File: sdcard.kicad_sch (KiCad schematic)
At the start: 20 parts, among them J9 microSD push-pull, Q2 -20V 2.3A P-ch, Q3 60V 300mA N-ch

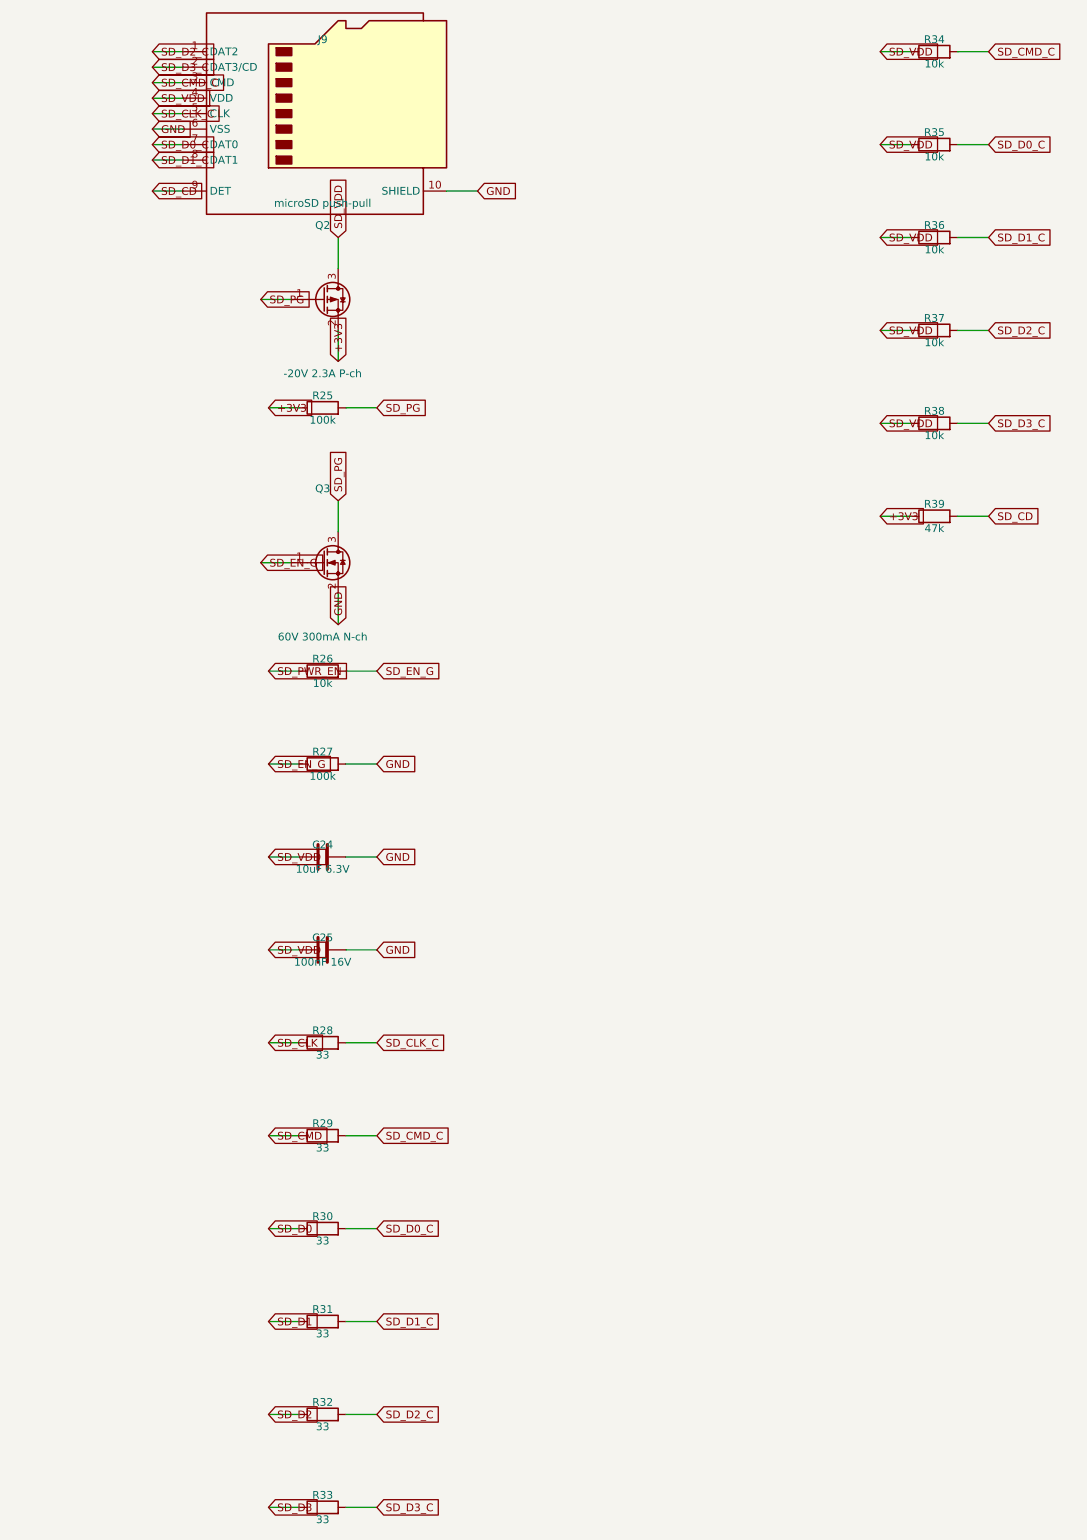
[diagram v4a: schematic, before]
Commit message: Schematic: power symbols and readable text placement (items 1-2 of 5)
The schematic was a netlist drawn as a picture: 486 global labels for 108
nets, roughly four per net, every part an island with a name flag on each
pin and no wires between anything. You could not trace a circuit by eye.
That is a fair description of a document that fails at the one thing a
schematic is for, and it is on me -- the generator was built to produce a
correct netlist and the drawing was an afterthought.

Two of the five agreed fixes are in:

Rails are power symbols. GND, +3V3, +5V, +5VS, +VBAT, VBUS and SD_VDD now
carry a proper power symbol instead of a net-name label -- 190 of them,
taking the label count from 486 to 296. Where KiCad has no stock symbol
for a rail a generic one is instantiated with its Value overridden, which
is how KiCad names a power net; validate.py re-extracts through KiCad and
compares node-for-node, so a wrong guess there would fail the build rather
than quietly merge two rails. PWR_FLAG keeps a label: pairing it with a
power symbol makes an island of two symbols that declares a rail and
connects to nothing visible.

Text no longer collides. Labels were all justified left, so any label
pointing back at its own component ran its text over the body -- RON_5V
across R4, SW_5V across L1; they now justify away from the part.
Reference and value sat hard against the symbol, so a pin leaving the top
or bottom put its stub and power symbol straight through them: "LM5164
(5V)" printed through the GND symbol under U2. Both now clear the stub,
and the row height accounts for it so the clearance does not just push
the collision into the next row. Power symbol references are hidden, as
they are in every schematic.

Also fixed: the packer wrapped on height but never on width, so the power
sheet silently ran off the 420 mm page -- two symbols landed at x = 422.9
where ERC reported them unconnected and nothing else complained. It now
fails loudly.

Items 3-5 (real hierarchy, w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
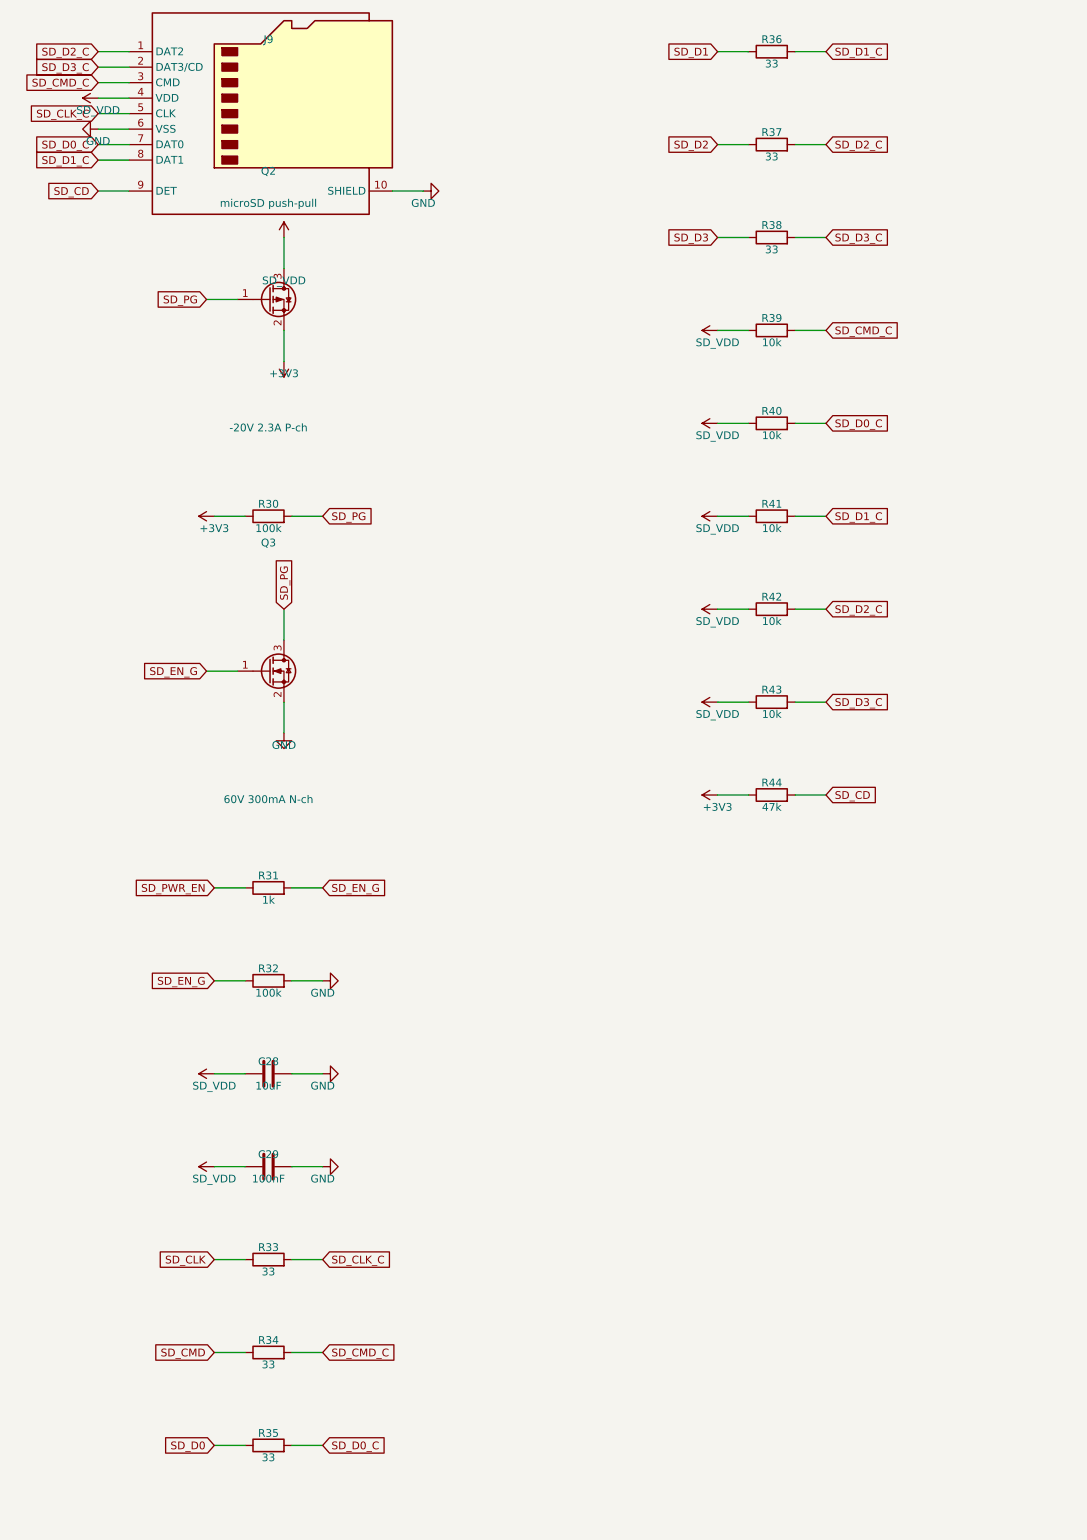
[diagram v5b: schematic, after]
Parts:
- removed C24: 10uF 6.3V, Capacitor_SMD:C_1206_3216Metric, symbol Device:C
- removed C25: 100nF 16V, Capacitor_SMD:C_0805_2012Metric, symbol Device:C
- removed R25, R27: 100k, Resistor_SMD:R_0805_2012Metric, symbol Device:R
- removed R26: 10k, Resistor_SMD:R_0805_2012Metric, symbol Device:R
- removed R28, R29: 33, Resistor_SMD:R_0805_2012Metric, symbol Device:R
- added C28: 10uF, Capacitor_SMD:C_1206_3216Metric, symbol Device:C
- added C29: 100nF, Capacitor_SMD:C_0805_2012Metric, symbol Device:C
- added R40, R41, R42, R43: 10k, Resistor_SMD:R_0805_2012Metric, symbol Device:R
- added R44: 47k, Resistor_SMD:R_0805_2012Metric, symbol Device:R
- Q3: Note Level shift for the P-ch gate -> Level shift for the P-ch gate. Prefer an AEC-Q101 equivalen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
- R30: value 33 -> 100k; Note Series damping -> Default off
- R31: value 33 -> 1k; Note Series damping -> Series gate resistor. 10k here divided against R27 100k and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
- R32: value 33 -> 100k; Note Series damping -> (none)
- R34, R35, R36, R37, R38: value 10k -> 33; Note Espressif's recommended value; pulled to the switched rail 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 -> Series damping
- R39: value 47k -> 10k; Note Card-detect pull-up -> Espressif's recommended value; pulled to the switched rail 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
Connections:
- net +3V3: now also R30.1, R44.1; no longer R39.1
- net GND: now also R32.2, C28.2, C29.2
- net SD_CD: now also R44.2; no longer R39.2
- net SD_CLK: now also R33.1
- net SD_CLK_C: now also R33.2
- net SD_CMD: now also R34.1
- net SD_CMD_C: now also R39.2
- net SD_D0: now also R35.1; no longer R30.1
- net SD_D0_C: now also R40.2; no longer R30.2
- net SD_D1: now also R36.1; no longer R31.1
- net SD_D1_C: now also R41.2; no longer R31.2
- net SD_D2: now also R37.1; no longer R32.1
- net SD_D2_C: now also R42.2; no longer R32.2
- net SD_D3: now also R38.1; no longer R33.1
- net SD_D3_C: now also R43.2; no longer R33.2
- net SD_EN_G: now also R31.2, R32.1
- net SD_PG: now also R30.2
- net SD_PWR_EN: now also R31.1
- net SD_VDD: now also R39.1, C28.1, C29.1, R40.1, R41.1, R42.1, R43.1; no longer R34.1, R35.1, R36.1, R37.1, R38.1
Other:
- moved on the sheet: J9, Q2, Q3, R30, R31, R32, R33, R34, R35, R36, R37, R38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

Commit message: Rev B is fully routed: zero DRC errors, nothing unconnected
84 x 84 mm, 1447 tracks, 258 vias, 179 footprints, 106 nets.

The last few connections were never routing problems. Each one was a part
sited away from the net it belongs to, and the autorouter reporting "no
path at any width" was telling the truth:

  +5VS  the sensor rail's source (PF1/FB2/D3) sat on the right beside the
        WS2812 header while everything it feeds -- the sensor harness and
        all four channel pull-ups -- is on the left. The net existed as
        two complete halves with a 45 mm gap through buck islands and the
        SD socket. Moved the source to the harness side.
  IO46  the strapping pull-downs were parked in the bottom band while
        IO3/IO45/IO46 run from the module's south pads to J7 at the top
        left, so R29 needed a trace the length of the board to reach its
        own net. Moved them under the module's south pads.

Adding router passes had never touched either. Moving the parts fixed
both immediately -- worth remembering next time a net "cannot be routed".

Also in this pass:

  - One LED. D6 (amber) and D7 (blue) and their resistors are gone; D4
    green stays on +3V3, which is the right rail to watch because it only
    lights if the whole chain came through -- battery, ideal diode, both
    converters. That also retires review item 11.2.10, the blue emitter
    that would have been near-invisible on a 3.288 V rail.
  - J7 grows to six pins: the three strapping pins, the two GPIOs freed
    by the LEDs (IO15/IO16), and a ground pin. The missing ground was
    review item 13.4.13.
  - USB_CC1 gets a Fine netclass at 0.2 mm. There is no route at 0.25 mm
    -- the USB-C pads are on 0.5 mm pitch and will not pass it -- and CC
    carries under a milliamp through a 5.1k pull-down.
  - build_board.py takes a lock. Two builds sharing the board file is how
    one run died at "Specctra session import failed" after ten minutes,
    when a second build regenerated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
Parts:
- removed R43: 10k, Resistor_SMD:R_0805_2012Metric, symbol Device:R
- removed R44: 47k, Resistor_SMD:R_0805_2012Metric, symbol Device:R
- added R28: 100k, Resistor_SMD:R_0805_2012Metric, symbol Device:R
- added R29: 1k, Resistor_SMD:R_0805_2012Metric, symbol Device:R
- R30: Note Default off -> (none)
- R31: value 1k -> 33; Note Series gate resistor. 10k here divided against R27 100k and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 -> Series damping
- R32: value 100k -> 33; Note (none) -> Series damping
- R37, R38: value 33 -> 10k; Note Series damping -> Espressif's recommended value; pulled to the switched rail 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
- R42: value 10k -> 47k; Note Espressif's recommended value; pulled to the switched rail 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 -> Card-detect pull-up
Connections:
- net +3V3: now also R42.1, R28.1; no longer R30.1
- net GND: now also R30.2; no longer R32.2
- net SD_CD: now also R42.2
- net SD_CLK: now also R31.1; no longer R33.1
- net SD_CLK_C: now also R31.2; no longer R33.2
- net SD_CMD: now also R32.1; no longer R34.1
- net SD_CMD_C: now also R32.2, R37.2; no longer R34.2, R39.2
- net SD_D0: now also R33.1; no longer R35.1
- net SD_D0_C: now also R33.2, R38.2; no longer R35.2, R40.2
- net SD_D1: now also R34.1; no longer R36.1
- net SD_D1_C: now also R34.2, R39.2; no longer R36.2, R41.2
- net SD_D2: now also R35.1; no longer R37.1
- net SD_D2_C: now also R35.2, R40.2; no longer R37.2, R42.2
- net SD_D3: now also R36.1; no longer R38.1
- net SD_D3_C: now also R36.2, R41.2; no longer R38.2
- net SD_EN_G: now also R30.1, R29.2; no longer R31.2, R32.1
- net SD_PG: now also R28.2; no longer R30.2
- net SD_PWR_EN: now also R29.1; no longer R31.1
- net SD_VDD: now also R37.1, R38.1; no longer R42.1
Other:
- moved on the sheet: R30, R31, R32, R33, R34, R35, R36, R37, R38, R39, R40, R41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
